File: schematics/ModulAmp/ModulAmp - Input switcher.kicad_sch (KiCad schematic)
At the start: 21 parts, among them J1 LINE IN 1, J2 LINE IN 2, J3 STREAM, J4 OUT, J5 +5v, J6 CONTROL, K1 LINE 1 RIGHT, K2 LINE 1 LEFT, K3 LINE 2 RIGHT, K4 LINE 2 LEFT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

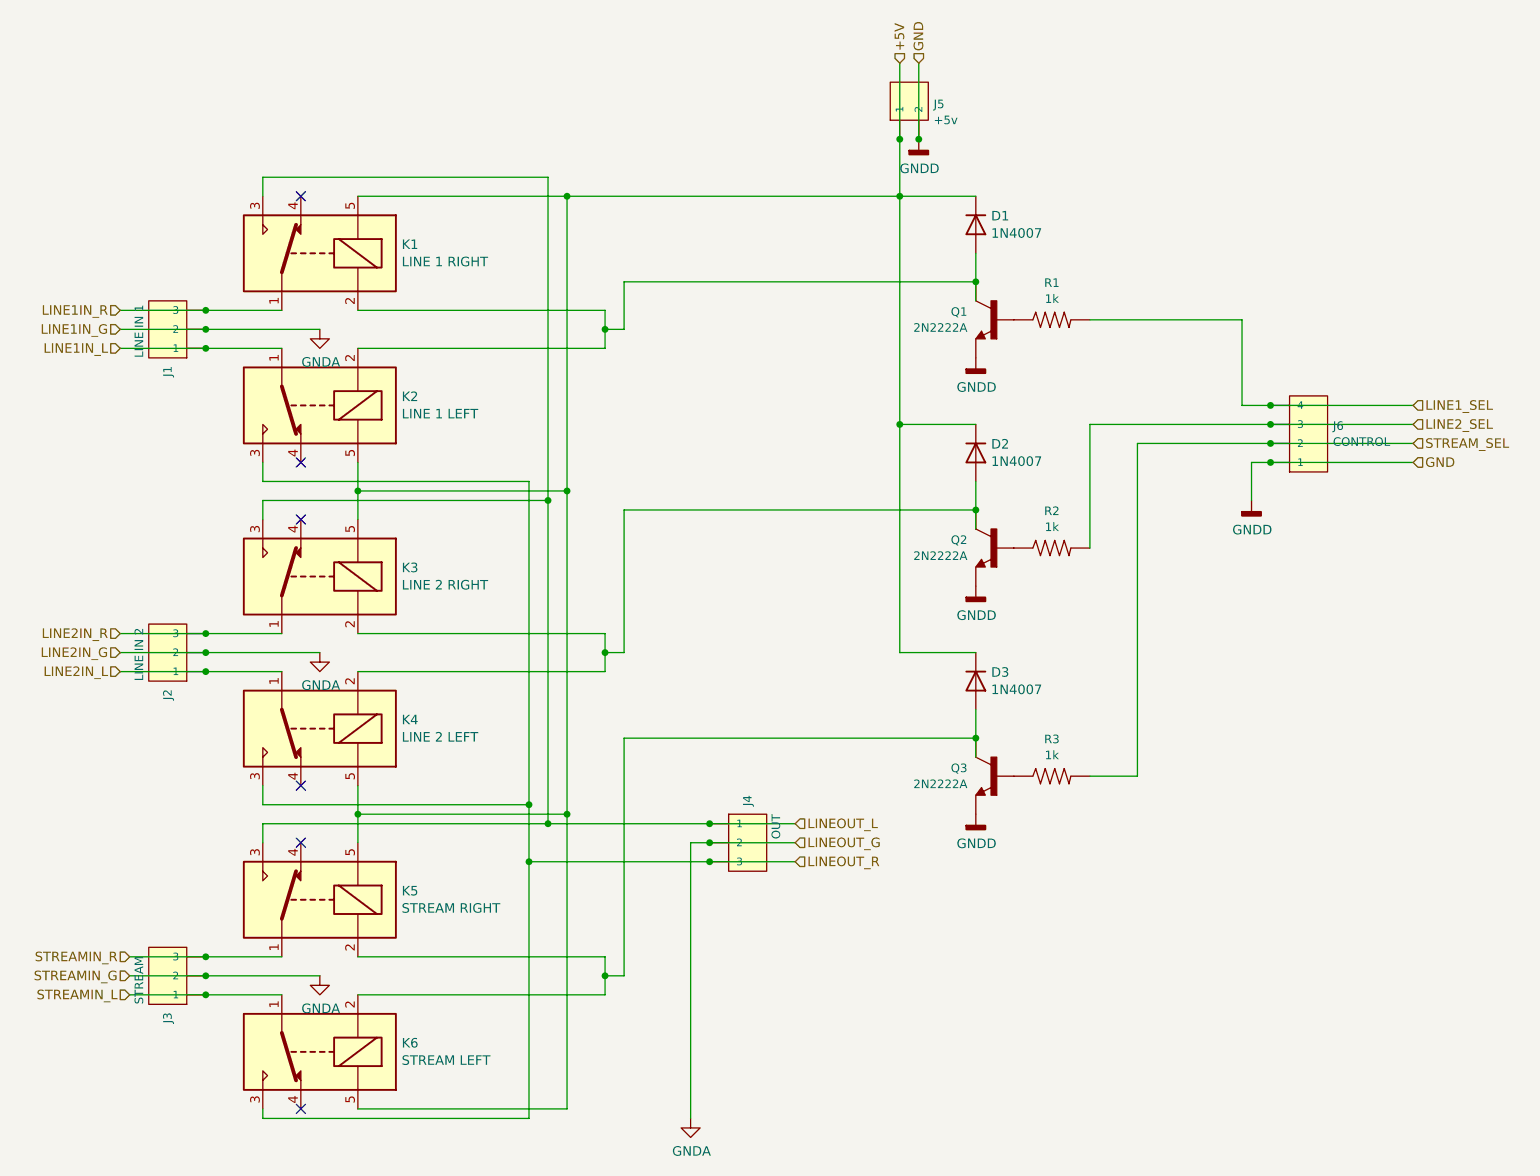
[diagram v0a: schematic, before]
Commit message: Refactored strings and added DHTxx full support
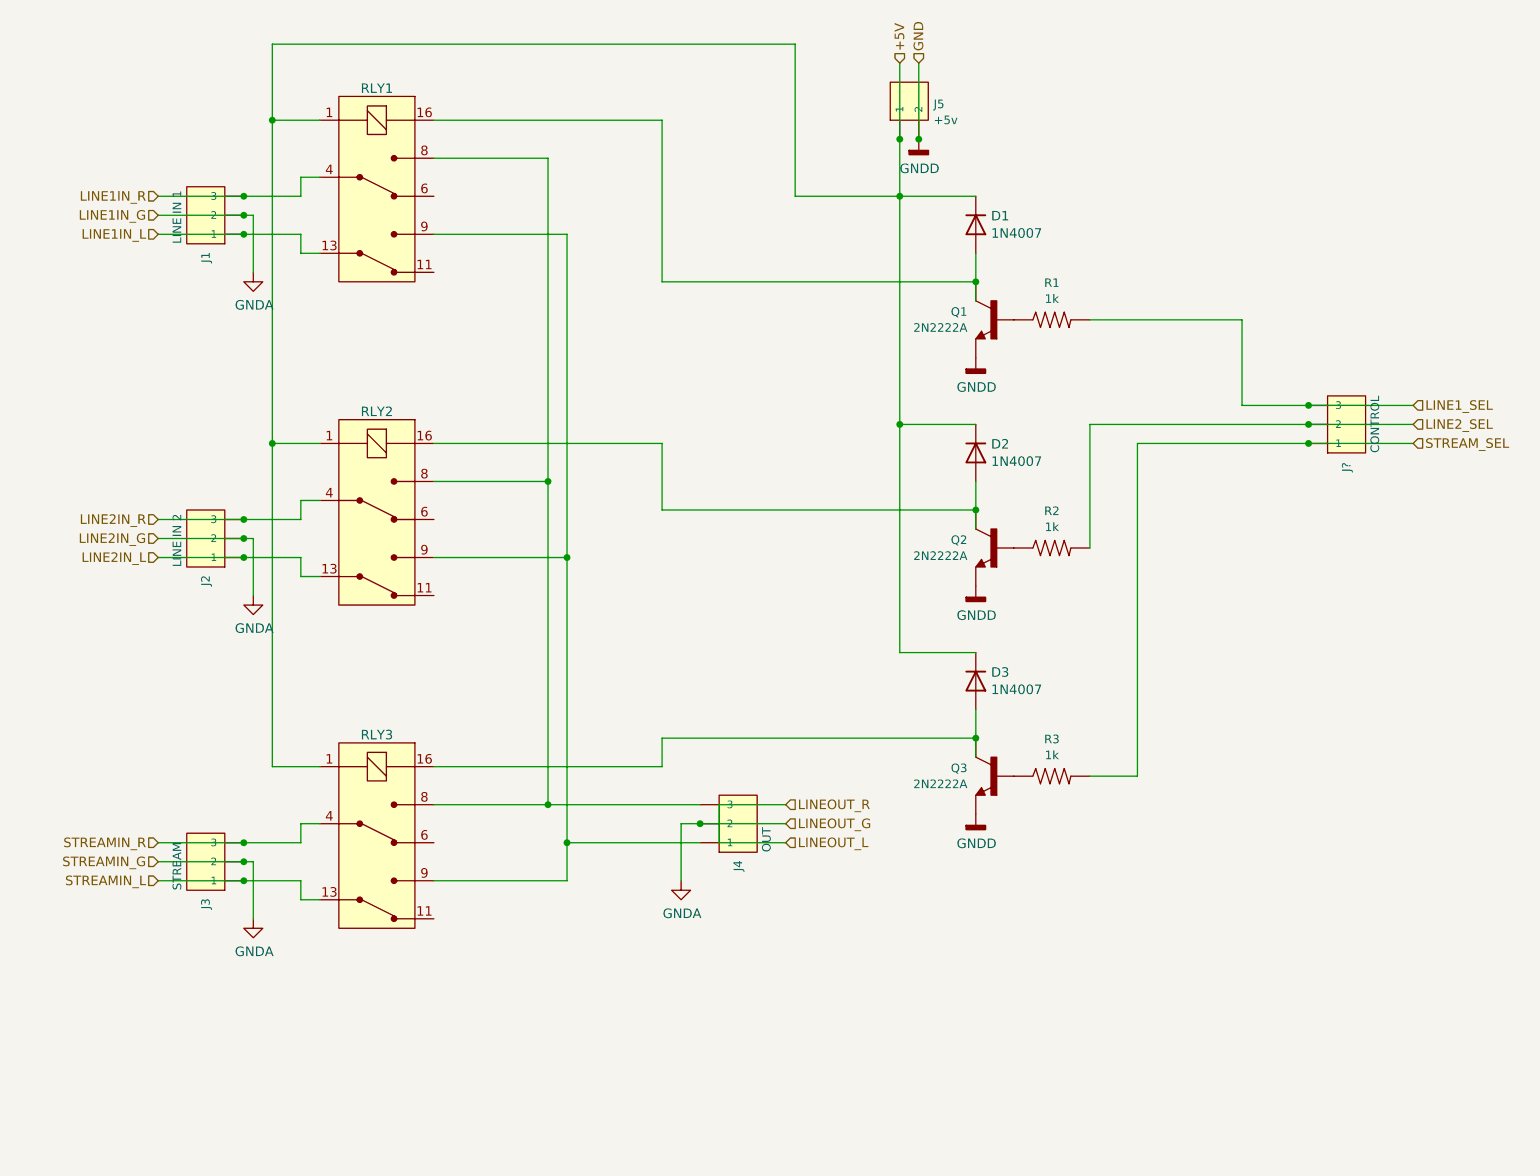
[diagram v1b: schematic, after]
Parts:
- removed J6: CONTROL, JST-4-PTH-VERT, symbol SparkFun-Connectors:CONN_04JST-PTH-VERT
- removed K1: LINE 1 RIGHT, Relay_THT:Relay_SPDT_SANYOU_SRD_Series_Form_C, symbol Relay:SANYOU_SRD_Form_C
- removed K2: LINE 1 LEFT, Relay_THT:Relay_SPDT_SANYOU_SRD_Series_Form_C, symbol Relay:SANYOU_SRD_Form_C
- removed K3: LINE 2 RIGHT, Relay_THT:Relay_SPDT_SANYOU_SRD_Series_Form_C, symbol Relay:SANYOU_SRD_Form_C
- removed K4: LINE 2 LEFT, Relay_THT:Relay_SPDT_SANYOU_SRD_Series_Form_C, symbol Relay:SANYOU_SRD_Form_C
- removed K5: STREAM RIGHT, Relay_THT:Relay_SPDT_SANYOU_SRD_Series_Form_C, symbol Relay:SANYOU_SRD_Form_C
- removed K6: STREAM LEFT, Relay_THT:Relay_SPDT_SANYOU_SRD_Series_Form_C, symbol Relay:SANYOU_SRD_Form_C
- added J?: CONTROL, JST-3-PTH-VERT, symbol SparkFun-Connectors:CONN_03JST-PTH-VERT
- added RLY1, RLY2, RLY3: G5V-2-DC12, digikey-footprints:Relay_THT_G5V-2, symbol dk_Signal-Relays-Up-to-2-Amps:G5V-2-DC12
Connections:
- net +5V: now also RLY1.1 (COIL), RLY2.1 (COIL), RLY3.1 (COIL)
- net LINE1IN_L: now also RLY1.13 (COM2)
- net LINE1IN_R: now also RLY1.4 (COM1)
- net LINE1_SEL: now also J?.3
- net LINE2IN_L: now also RLY2.13 (COM2)
- net LINE2IN_R: now also RLY2.4 (COM1)
- net LINE2_SEL: now also J?.2
- net LINEOUT_L: no longer J4.1
- net STREAMIN_L: now also RLY3.13 (COM2)
- net STREAMIN_R: now also RLY3.4 (COM1)
- net STREAM_SEL: now also J?.1
- net at D3.2 (A), Q3.1 (C): now also RLY3.16 (COIL)
- net at D2.2 (A), Q2.1 (C): now also RLY2.16 (COIL)
- net at D1.2 (A), Q1.1 (C): now also RLY1.16 (COIL)
- net LINEOUT_R: no longer names the net of J4.3
- net LINEOUT_R: now also RLY1.8 (NO1), RLY2.8 (NO1), RLY3.8 (NO1)
- new net: J4.1, RLY1.9 (NO2), RLY2.9 (NO2), RLY3.9 (NO2)
- no-connect marks 6 -> 0
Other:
- moved on the sheet: J1, J2, J3, J4
